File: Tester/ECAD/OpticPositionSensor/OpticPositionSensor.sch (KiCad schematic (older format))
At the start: 14 parts, among them J1 Conn_01x10_Male, U1 TLV70019_SOT23-5, U2 PMW3360DM-T2QU, U3 SN74LVC1T45DBV, U4 SN74LVC1T45DBV, U5 SN74LVC1T45DBV, U6 SN74LVC1T45DBV, U7 SN74LVC1T45DBV, U8 SN74LVC1T45DBV

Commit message: Assigned footprints.
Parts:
- C1, C2, C3, C4: footprint (none) -> Capacitor_SMD:C_0805_2012Metric_Pad1.15x1.40mm_HandSolder
- R1: footprint (none) -> Resistor_SMD:R_0805_2012Metric_Pad1.15x1.40mm_HandSolder
- U1: footprint Package_TO_SOT_SMD:SOT-23-5 -> Package_TO_SOT_SMD:SOT-23-5_HandSoldering
- U3, U4, U5, U6, U7, U8: footprint Package_TO_SOT_SMD:SOT-23-6 -> Package_TO_SOT_SMD:SOT-23-6_Handsoldering
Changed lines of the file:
@@
 F 0 "C1" H 1315 6196 50  0000 L CNN
 F 1 "4.7uC" H 1315 6105 50  0000 L CNN
-F 2 "" H 1238 6000 50  0001 C CNN
+F 2 "Capacitor_SMD:C_0805_2012Metric_Pad1.15x1.40mm_HandSolder" H 1238 6000 50  0001 C CNN
 F 3 "~" H 1200 6150 50  0001 C CNN
 	1    1200 6150
@@
 F 0 "C3" H 1765 6196 50  0000 L CNN
 F 1 "100nC" H 1765 6105 50  0000 L CNN
-F 2 "" H 1688 6000 50  0001 C CNN
+F 2 "Capacitor_SMD:C_0805_2012Metric_Pad1.15x1.40mm_HandSolder" H 1688 6000 50  0001 C CNN
 F 3 "~" H 1650 6150 50  0001 C CNN
 	1    1650 6150
@@
 F 0 "U4" H 5050 2900 50  0000 L CNN
 F 1 "SN74LVC1T45DBV" H 5050 2200 50  0000 L CNN
-F 2 "Package_TO_SOT_SMD:SOT-23-6" H 4750 2100 50  0001 C CNN
+F 2 "Package_TO_SOT_SMD:SOT-23-6_Handsoldering" H 4750 2100 50  0001 C CNN
 F 3 "http://www.ti.com/lit/ds/symlink/sn74lvc1t45.pdf" H 3850 1900 50  0001 C CNN
 	1    4750 2550
@@
 F 0 "U5" H 5050 3950 50  0000 L CNN
 F 1 "SN74LVC1T45DBV" H 5050 3250 50  0000 L CNN
-F 2 "Package_TO_SOT_SMD:SOT-23-6" H 4750 3150 50  0001 C CNN
+F 2 "Package_TO_SOT_SMD:SOT-23-6_Handsoldering" H 4750 3150 50  0001 C CNN
 F 3 "http://www.ti.com/lit/ds/symlink/sn74lvc1t45.pdf" H 3850 2950 50  0001 C CNN
 	1    4750 3600
@@
 F 0 "U8" H 5050 7050 50  0000 L CNN
 F 1 "SN74LVC1T45DBV" H 5050 6350 50  0000 L CNN
-F 2 "Package_TO_SOT_SMD:SOT-23-6" H 4750 6250 50  0001 C CNN
+F 2 "Package_TO_SOT_SMD:SOT-23-6_Handsoldering" H 4750 6250 50  0001 C CNN
 F 3 "http://www.ti.com/lit/ds/symlink/sn74lvc1t45.pdf" H 3850 6050 50  0001 C CNN
 	1    4750 6700
@@
 F 0 "U7" H 5050 5950 50  0000 L CNN
 F 1 "SN74LVC1T45DBV" H 5050 5250 50  0000 L CNN
-F 2 "Package_TO_SOT_SMD:SOT-23-6" H 4750 5150 50  0001 C CNN
+F 2 "Package_TO_SOT_SMD:SOT-23-6_Handsoldering" H 4750 5150 50  0001 C CNN
 F 3 "http://www.ti.com/lit/ds/symlink/sn74lvc1t45.pdf" H 3850 4950 50  0001 C CNN
 	1    4750 5600
@@
 F 0 "U6" H 5050 4950 50  0000 L CNN
 F 1 "SN74LVC1T45DBV" H 5050 4250 50  0000 L CNN
-F 2 "Package_TO_SOT_SMD:SOT-23-6" H 4750 4150 50  0001 C CNN
+F 2 "Package_TO_SOT_SMD:SOT-23-6_Handsoldering" H 4750 4150 50  0001 C CNN
 F 3 "http://www.ti.com/lit/ds/symlink/sn74lvc1t45.pdf" H 3850 3950 50  0001 C CNN
 	1    4750 4600
@@
 F 0 "U3" H 5050 1750 50  0000 L CNN
 F 1 "SN74LVC1T45DBV" H 5050 1050 50  0000 L CNN
-F 2 "Package_TO_SOT_SMD:SOT-23-6" H 4750 950 50  0001 C CNN
+F 2 "Package_TO_SOT_SMD:SOT-23-6_Handsoldering" H 4750 950 50  0001 C CNN
 F 3 "http://www.ti.com/lit/ds/symlink/sn74lvc1t45.pdf" H 3850 750 50  0001 C CNN
 	1    4750 1400
@@
 F 0 "U1" H 2300 1450 50  0000 C CNN
 F 1 "TLV70019_SOT23-5" H 2200 1950 50  0000 C CNN
-F 2 "Package_TO_SOT_SMD:SOT-23-5" H 2050 2025 50  0001 C CIN
+F 2 "Package_TO_SOT_SMD:SOT-23-5_HandSoldering" H 2050 2025 50  0001 C CIN
 F 3 "http://www.ti.com/lit/ds/symlink/tlv700.pdf" H 2050 1750 50  0001 C CNN
 	1    2050 1700
@@
 F 0 "C4" H 2665 1896 50  0000 L CNN
 F 1 "1uC" H 2665 1805 50  0000 L CNN
-F 2 "" H 2588 1700 50  0001 C CNN
+F 2 "Capacitor_SMD:C_0805_2012Metric_Pad1.15x1.40mm_HandSolder" H 2588 1700 50  0001 C CNN
 F 3 "~" H 2550 1850 50  0001 C CNN
 	1    2550 1850
@@
 F 0 "C2" H 1415 1896 50  0000 L CNN
 F 1 "1uC" H 1415 1805 50  0000 L CNN
-F 2 "" H 1338 1700 50  0001 C CNN
+F 2 "Capacitor_SMD:C_0805_2012Metric_Pad1.15x1.40mm_HandSolder" H 1338 1700 50  0001 C CNN
 F 3 "~" H 1300 1850 50  0001 C CNN
 	1    1300 1850
@@
 F 0 "R1" H 2970 3446 50  0000 L CNN
 F 1 "39R" H 2970 3355 50  0000 L CNN
-F 2 "" V 2830 3400 50  0001 C CNN
+F 2 "Resistor_SMD:R_0805_2012Metric_Pad1.15x1.40mm_HandSolder" V 2830 3400 50  0001 C CNN
 F 3 "~" H 2900 3400 50  0001 C CNN
 	1    2900 3400

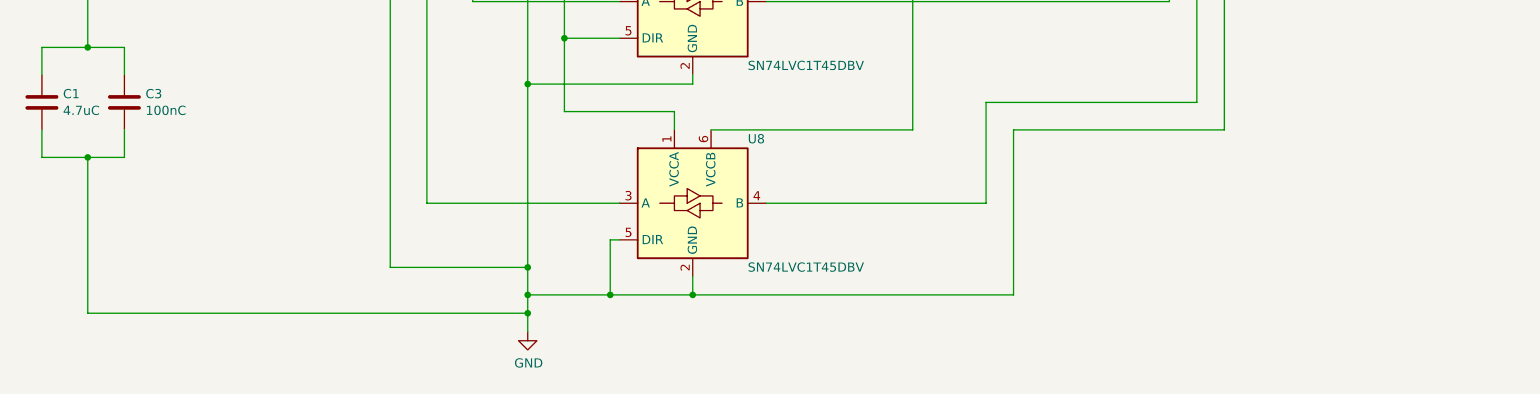
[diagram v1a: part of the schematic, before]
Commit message: Progressed PCD pad.
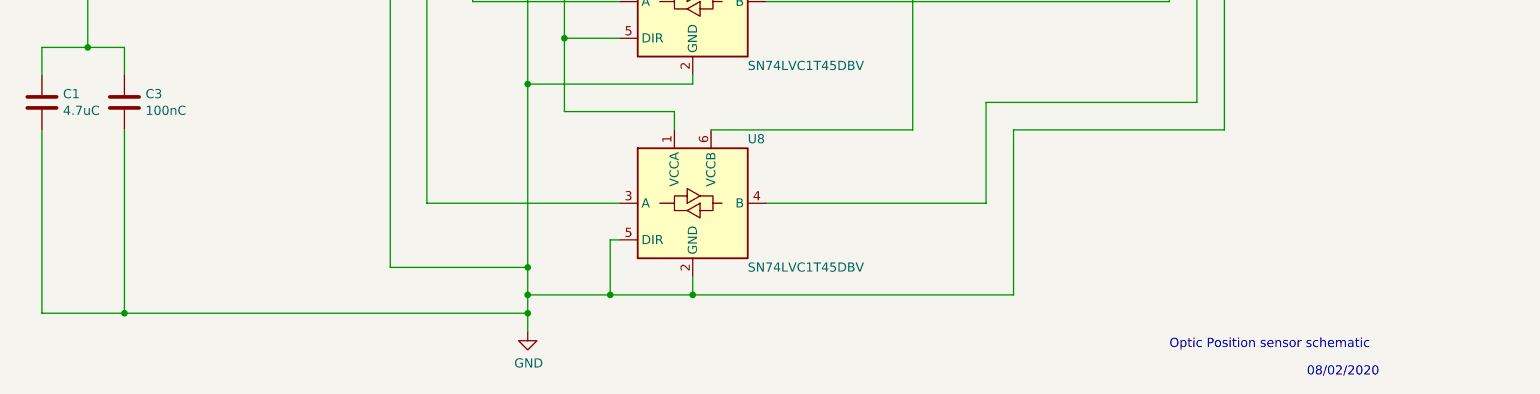
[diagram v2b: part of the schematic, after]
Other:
- note added: "08/02/2020"
- note added: "Optic Position sensor schematic"
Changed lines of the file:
@@
 ~NRESET
-Wire Wire Line
-	3850 7400 3850 7300
 Wire Wire Line
 	3850 1950 4300 1950
@@
 GND
 Wire Wire Line
-	1200 6300 1200 6450
-Wire Wire Line
-	1200 6450 1450 6450
-Wire Wire Line
-	1650 6450 1650 6300
-Wire Wire Line
 	1650 6000 1650 5850
 Wire Wire Line
@@
 Wire Wire Line
 	1450 5850 1200 5850
-Wire Wire Line
-	1450 6450 1450 7300
-Wire Wire Line
-	1450 7300 3850 7300
-Connection ~ 1450 6450
-Wire Wire Line
-	1450 6450 1650 6450
-Connection ~ 3850 7300
-Wire Wire Line
-	3850 7300 3850 7200
 Wire Wire Line
 	1700 4050 1600 4050
@@
 Wire Wire Line
 	2050 2200 2550 2200
+Wire Wire Line
+	3850 7200 3850 7300
+Wire Wire Line
+	1200 6300 1200 7300
+Wire Wire Line
+	1200 7300 1650 7300
+Connection ~ 3850 7300
+Wire Wire Line
+	3850 7300 3850 7400
+Wire Wire Line
+	1650 6300 1650 7300
+Connection ~ 1650 7300
+Wire Wire Line
+	1650 7300 3850 7300
+Text Notes 8100 7650 0    50   ~ 0
+08/02/2020
+Text Notes 7350 7500 0    50   ~ 0
+Optic Position sensor schematic
 $EndSCHEMATC

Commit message: Progressed PCB design.
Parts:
- added H1, H2, H3, H4: MountingHole, MountingHole:MountingHole_3.2mm_M3_Pad, symbol Mechanical:MountingHole
- J1: footprint (none) -> Connector_Molex:Molex_PicoBlade_53048-1010_1x10_P1.25mm_Horizontal
- U2: footprint (none) -> PixArt:PMW3360DM-T2QU
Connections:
- net ~NCS_HEADER: now reaches J1.2 (Pin_2), U3.4 (B)
- net MISO_HEADER: now reaches J1.3 (Pin_3), U4.4 (B)
- net MOSI_HEADER: now reaches J1.5 (Pin_5), U5.4 (B)
- net ~NRESET_HEADER: now reaches J1.9 (Pin_9), U8.4 (B)
- net MOTION_HEADER: now reaches J1.8 (Pin_8), U7.4 (B)
- net SCLK_HEADER: now reaches J1.7 (Pin_7), U6.4 (B)
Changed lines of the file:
@@
 F 0 "U2" H 1850 4800 50  0000 C CNN
 F 1 "PMW3360DM-T2QU" H 2150 3850 50  0000 C CNN
-F 2 "" H 2150 4200 50  0001 C CNN
+F 2 "PixArt:PMW3360DM-T2QU" H 2150 4200 50  0001 C CNN
 F 3 "" H 2150 4200 50  0001 C CNN
 	1    2150 4200
@@
 F 0 "J1" H 8472 3474 50  0000 R CNN
 F 1 "Conn_01x10_Male" H 8472 3383 50  0000 R CNN
-F 2 "" H 8500 3500 50  0001 C CNN
+F 2 "Connector_Molex:Molex_PicoBlade_53048-1010_1x10_P1.25mm_Horizontal" H 8500 3500 50  0001 C CNN
 F 3 "~" H 8500 3500 50  0001 C CNN
 	1    8500 3500
@@
 Text Notes 7350 7500 0    50   ~ 0
 Optic Position sensor schematic
+$Comp
+L Mechanical:MountingHole H1
+U 1 1 5E417948
+P 9700 1650
+F 0 "H1" H 9800 1696 50  0000 L CNN
+F 1 "MountingHole" H 9800 1605 50  0000 L CNN
+F 2 "MountingHole:MountingHole_3.2mm_M3_Pad" H 9700 1650 50  0001 C CNN
+F 3 "~" H 9700 1650 50  0001 C CNN
+	1    9700 1650
+	1    0    0    -1
+$EndComp
+$Comp
+L Mechanical:MountingHole H2
+U 1 1 5E417FD8
+P 9700 1950
+F 0 "H2" H 9800 1996 50  0000 L CNN
+F 1 "MountingHole" H 9800 1905 50  0000 L CNN
+F 2 "MountingHole:MountingHole_3.2mm_M3_Pad" H 9700 1950 50  0001 C CNN
+F 3 "~" H 9700 1950 50  0001 C CNN
+	1    9700 1950
+	1    0    0    -1
+$EndComp
+$Comp
+L Mechanical:MountingHole H3
+U 1 1 5E4186E0
+P 9700 2250
+F 0 "H3" H 9800 2296 50  0000 L CNN
+F 1 "MountingHole" H 9800 2205 50  0000 L CNN
+F 2 "MountingHole:MountingHole_3.2mm_M3_Pad" H 9700 2250 50  0001 C CNN
+F 3 "~" H 9700 2250 50  0001 C CNN
+	1    9700 2250
+	1    0    0    -1
+$EndComp
+$Comp
+L Mechanical:MountingHole H4
+U 1 1 5E4188C7
+P 9700 2500
+F 0 "H4" H 9800 2546 50  0000 L CNN
+F 1 "MountingHole" H 9800 2455 50  0000 L CNN
+F 2 "MountingHole:MountingHole_3.2mm_M3_Pad" H 9700 2500 50  0001 C CNN
+F 3 "~" H 9700 2500 50  0001 C CNN
+	1    9700 2500
+	1    0    0    -1
+$EndComp
+Text Label 6400 1400 0    50   ~ 0
+~NCS_HEADER
+Text Label 6400 2550 0    50   ~ 0
+MISO_HEADER
+Text Label 6450 3600 0    50   ~ 0
+MOSI_HEADER
+Text Label 6500 4600 0    50   ~ 0
+SCLK_HEADER
+Text Label 6550 5600 0    50   ~ 0
+MOTION_HEADER
+Text Label 6550 6150 0    50   ~ 0
+~NRESET_HEADER
 $EndSCHEMATC

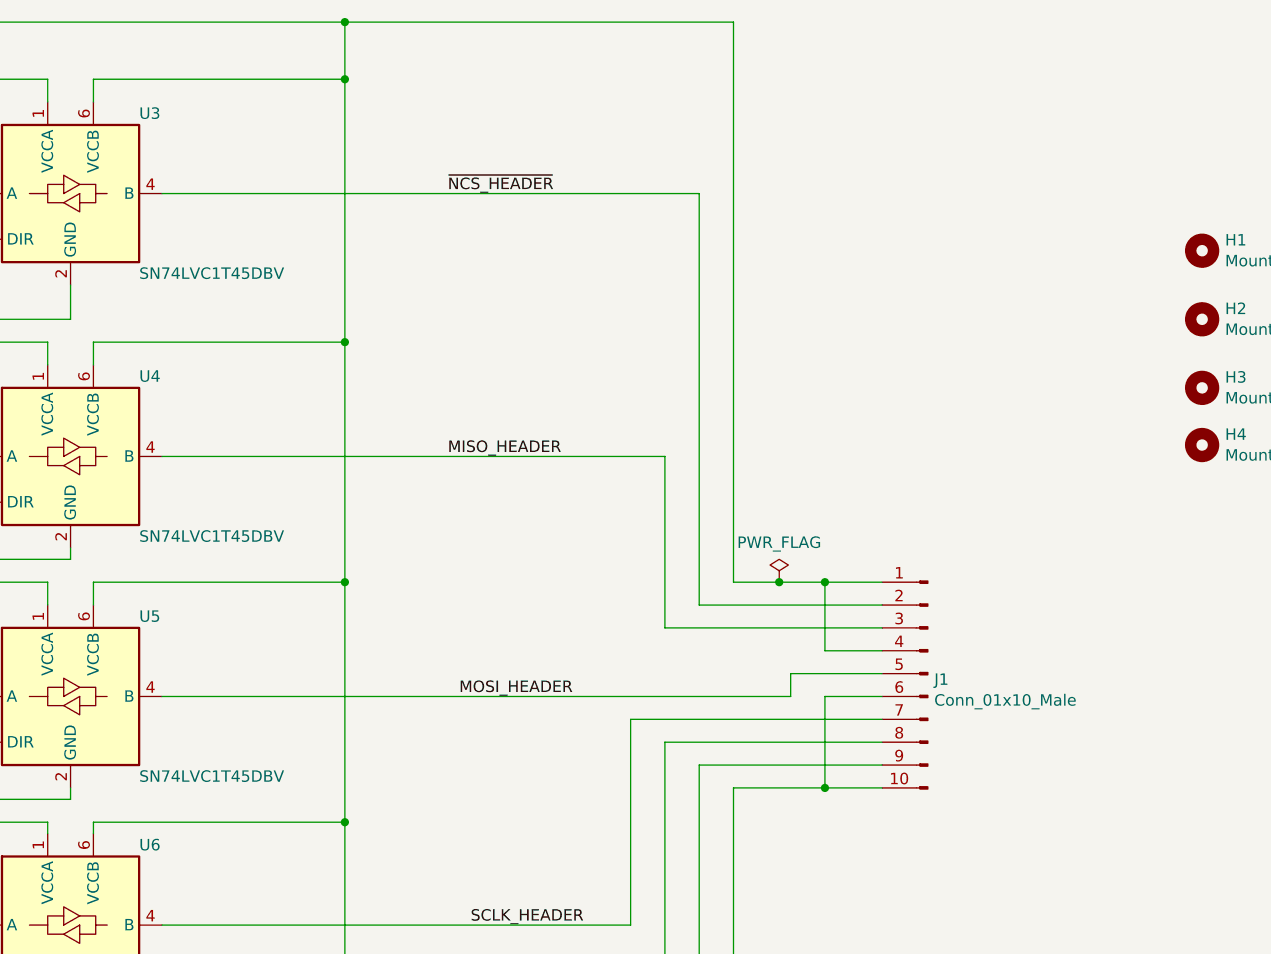
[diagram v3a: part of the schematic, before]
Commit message: Reworked Optical Sensor PCB.
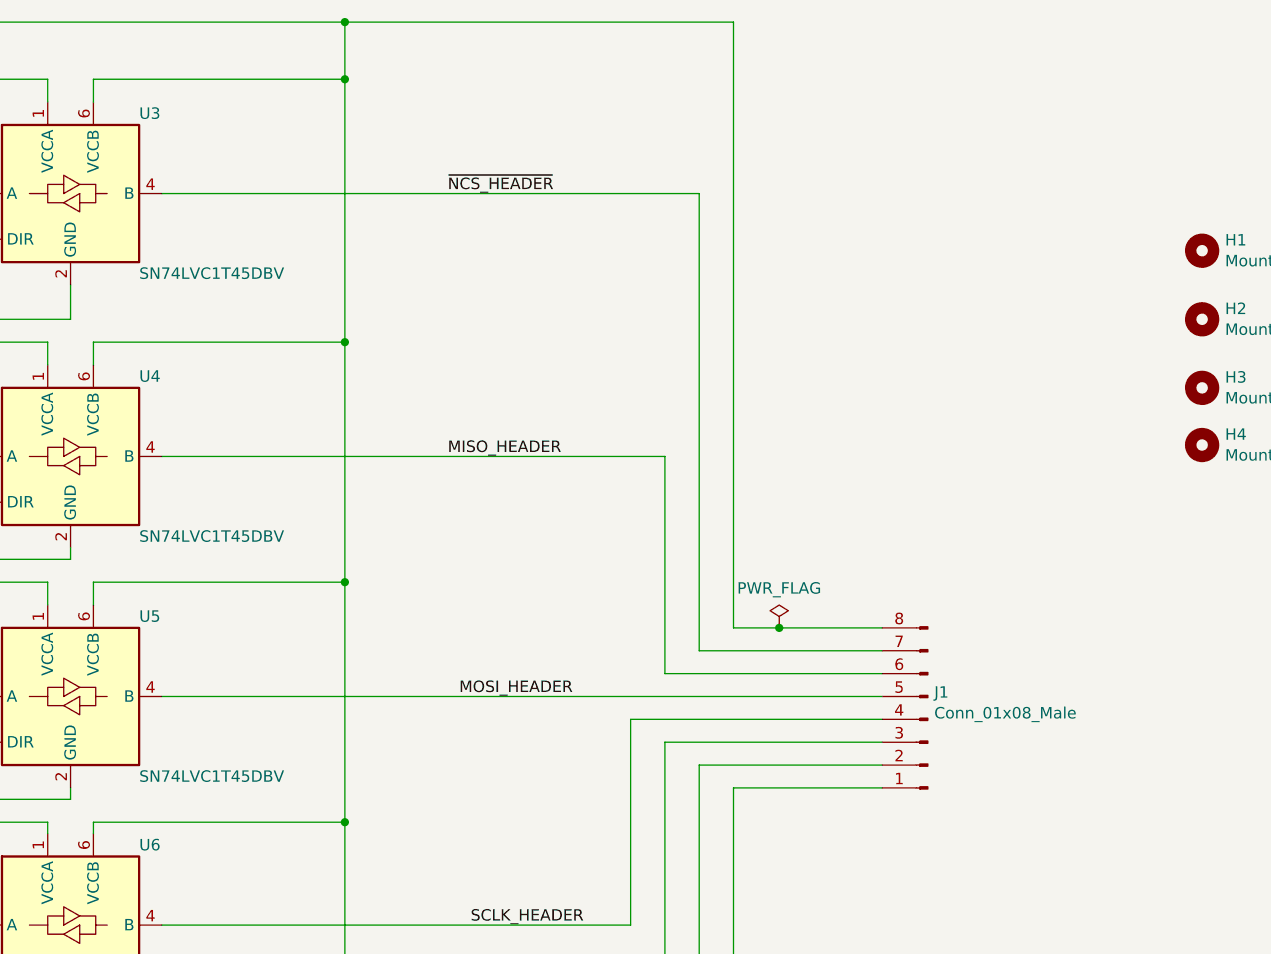
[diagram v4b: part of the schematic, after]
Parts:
- removed J1: Conn_01x10_Male, Connector_Molex:Molex_PicoBlade_53048-1010_1x10_P1.25mm_Horizontal, symbol Connector:Conn_01x10_Male
- added J1: Conn_01x08_Male, Connector_Molex:Molex_PicoBlade_53048-0810_1x08_P1.25mm_Horizontal, symbol Connector:Conn_01x08_Male
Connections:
- net GND: now also J1.1 (Pin_1)
- net MISO_HEADER: now also J1.6 (Pin_6)
- net MOSI_HEADER: now also J1.5 (Pin_5)
- net MOTION_HEADER: now also J1.3 (Pin_3)
- net SCLK_HEADER: now also J1.4 (Pin_4)
- net V_IN: now also J1.8 (Pin_8)
- net ~NCS_HEADER: now also J1.7 (Pin_7)
- net ~NRESET_HEADER: now also J1.2 (Pin_2)
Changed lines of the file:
@@
 Connection ~ 1300 1600
 Connection ~ 5950 900
-$Comp
-L Connector:Conn_01x10_Male J1
-U 1 1 5E4AD5A0
-P 8500 3500
-F 0 "J1" H 8472 3474 50  0000 R CNN
-F 1 "Conn_01x10_Male" H 8472 3383 50  0000 R CNN
-F 2 "Connector_Molex:Molex_PicoBlade_53048-1010_1x10_P1.25mm_Horizontal" H 8500 3500 50  0001 C CNN
-F 3 "~" H 8500 3500 50  0001 C CNN
-	1    8500 3500
-	-1   0    0    -1
-$EndComp
-Wire Wire Line
-	8300 4000 8050 4000
 Wire Wire Line
 	7650 4000 7650 6300
@@
 Connection ~ 4750 7200
 Wire Wire Line
-	8300 3100 8050 3100
-Wire Wire Line
-	7650 3100 7650 650
+	7650 3300 7650 650
 Wire Wire Line
 	7650 650  5950 650
@@
 Wire Wire Line
 	7500 6150 7500 3900
-Wire Wire Line
-	7500 3900 8300 3900
 Wire Wire Line
 	5150 5600 7350 5600
@@
 	7200 3700 8300 3700
 Wire Wire Line
-	8300 3600 8050 3600
-Wire Wire Line
-	8050 3600 8050 4000
-Connection ~ 8050 4000
-Wire Wire Line
-	8050 4000 7650 4000
-Wire Wire Line
-	5150 3600 7900 3600
-Wire Wire Line
-	7900 3600 7900 3500
-Wire Wire Line
-	7900 3500 8300 3500
-Wire Wire Line
 	5150 1400 7500 1400
 Wire Wire Line
-	7500 1400 7500 3200
+	7500 1400 7500 3400
 Wire Wire Line
-	7500 3200 8300 3200
+	7500 3400 8300 3400
 Wire Wire Line
 	5150 2550 7350 2550
 Wire Wire Line
-	7350 2550 7350 3300
+	7350 2550 7350 3500
 Wire Wire Line
-	7350 3300 8300 3300
-Wire Wire Line
-	8300 3400 8050 3400
-Wire Wire Line
-	8050 3400 8050 3100
-Connection ~ 8050 3100
-Wire Wire Line
-	8050 3100 7850 3100
+	7350 3500 8300 3500
 $Comp
 L power:PWR_FLAG #FLG0101
 U 1 1 5E50D827
-P 7850 3100
-F 0 "#FLG0101" H 7850 3175 50  0001 C CNN
-F 1 "PWR_FLAG" H 7850 3273 50  0000 C CNN
-F 2 "" H 7850 3100 50  0001 C CNN
-F 3 "~" H 7850 3100 50  0001 C CNN
-	1    7850 3100
+P 7850 3300
+F 0 "#FLG0101" H 7850 3375 50  0001 C CNN
+F 1 "PWR_FLAG" H 7850 3473 50  0000 C CNN
+F 2 "" H 7850 3300 50  0001 C CNN
+F 3 "~" H 7850 3300 50  0001 C CNN
+	1    7850 3300
 	1    0    0    -1
 $EndComp
-Connection ~ 7850 3100
+Connection ~ 7850 3300
 Wire Wire Line
-	7850 3100 7650 3100
+	7850 3300 7650 3300
 Wire Wire Line
 	1300 2200 2050 2200
@@
 Text Label 6550 6150 0    50   ~ 0
 ~NRESET_HEADER
+$Comp
+L Connector:Conn_01x08_Male J1
+U 1 1 5E497C0D
+P 8500 3700
+F 0 "J1" H 8472 3582 50  0000 R CNN
+F 1 "Conn_01x08_Male" H 8472 3673 50  0000 R CNN
+F 2 "Connector_Molex:Molex_PicoBlade_53048-0810_1x08_P1.25mm_Horizontal" H 8500 3700 50  0001 C CNN
+F 3 "~" H 8500 3700 50  0001 C CNN
+	1    8500 3700
+	-1   0    0    1
+$EndComp
+Wire Wire Line
+	7850 3300 8300 3300
+Wire Wire Line
+	7500 3900 8300 3900
+Wire Wire Line
+	7650 4000 8300 4000
+Wire Wire Line
+	5150 3600 8300 3600
 $EndSCHEMATC
